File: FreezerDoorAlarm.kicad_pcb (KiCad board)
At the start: 2 copper layers, 64 x 35 mm, 36 parts, among them J1 Barrel_Jack, J2 Conn_01x02_Female, J3 Conn_01x01, J4 Conn_01x01, Q1 MMBT3906, Q2 MMBT3904, Q3 MMBT3906, Q4 MMBT3904, Q5 BSS138, Q6 MMBT3906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

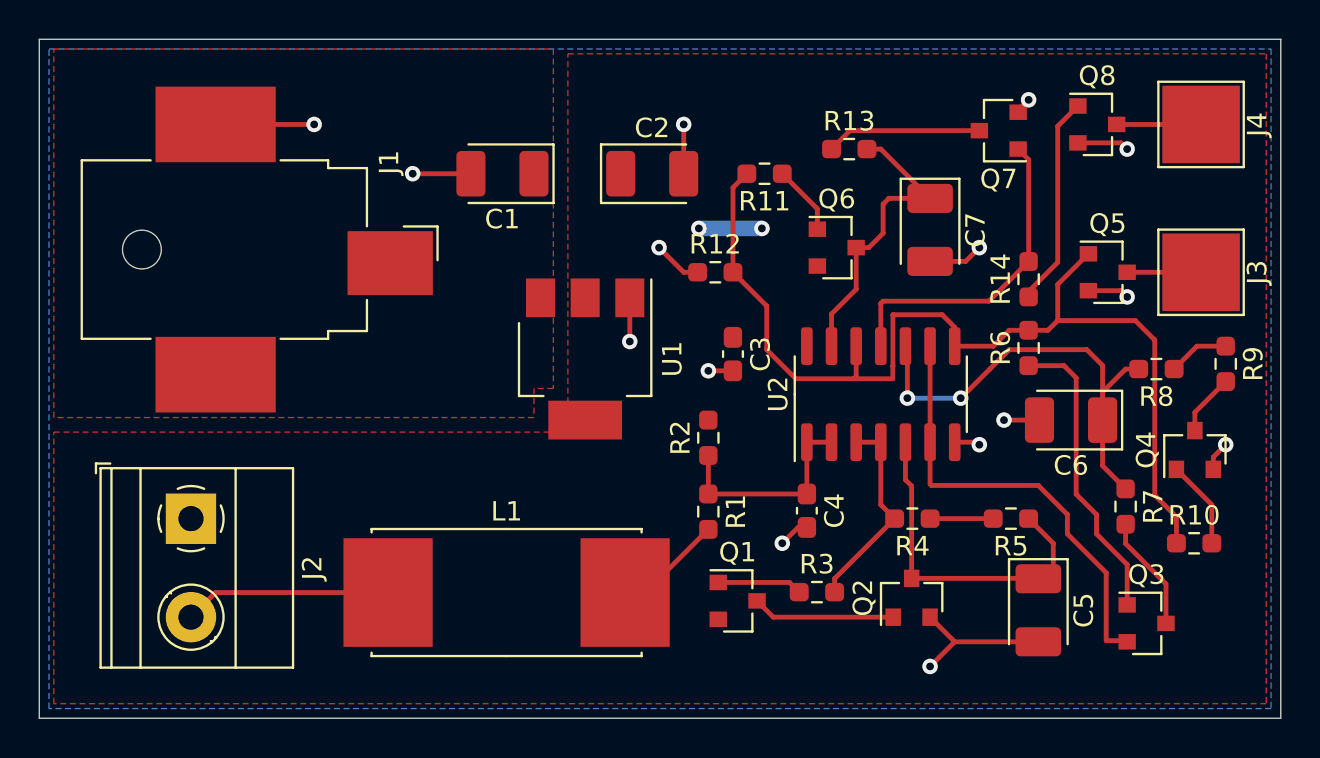
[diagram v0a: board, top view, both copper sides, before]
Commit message: Where large/fast currents are expected to flow (Q2/C5, U2 bypass) loop area has been reduced.
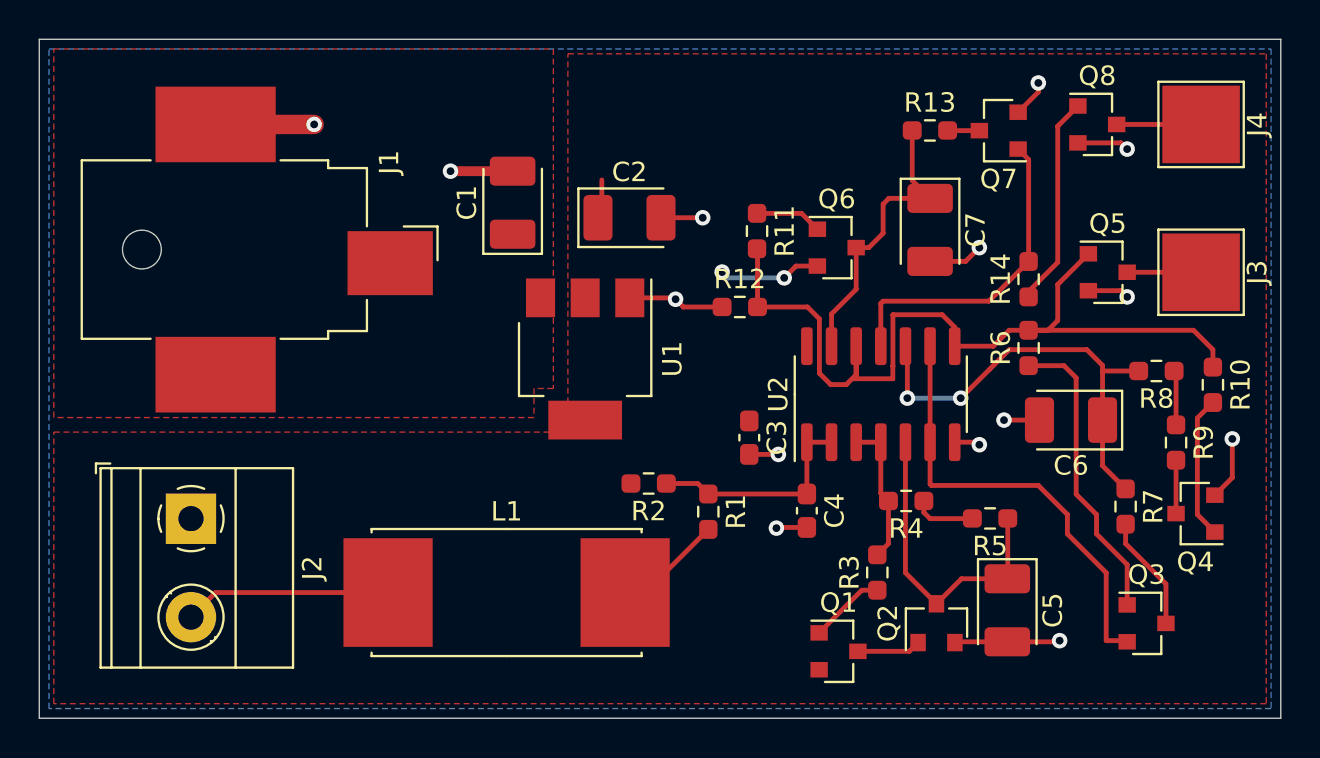
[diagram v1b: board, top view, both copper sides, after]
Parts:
- moved R10 8.22 mm to (136.5, 85.8), turned to 270 degrees
- moved Q1 5.81 mm to (117.2, 99.5)
- moved R9 4.80 mm to (134.6, 88.8)
- moved C3 4.39 mm to (112.6, 88.5)
- moved R13 4.27 mm to (121.9, 72.7)
- moved R2 3.88 mm to (107.4, 90.9), turned to 180 degrees
- moved Q4 3.28 mm to (135.6, 92.5), turned to 180 degrees
- moved R3 3.27 mm to (119.2, 95.5), turned to 90 degrees
- moved R11 2.98 mm to (113.0, 77.9), turned to 270 degrees
- moved C2 2.55 mm to (106.4, 77.2)
- moved R12 2.19 mm to (112.1, 81.8)
- moved Q2 1.83 mm to (122.2, 98.1)
- moved C5 1.60 mm to (125.9, 97.4)
- moved C1 1.58 mm to (100.4, 76.4), turned to 90 degrees
- moved R5 1.08 mm to (125.0, 92.7)
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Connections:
- R13 pad 1: Net-(Q7-Pad3) -> Net-(C7-Pad1)
- R13 pad 2: Net-(C7-Pad1) -> Net-(Q7-Pad3)
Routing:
- net Net-(Q5-Pad1): track 53.0 -> 45.3 mm
- net Net-(Q7-Pad3): track 8.01 -> 1.64 mm
- net +5V: track 3.25 -> 7.44 mm
- net Net-(Q1-Pad3): track 7.37 -> 3.29 mm
- net Net-(R3-Pad2): track 10.6 -> 7.48 mm
- net Net-(Q4-Pad1): track 4.57 -> 7.38 mm
- net Net-(C5-Pad1): track 17.3 -> 16.3 mm
- net GNDD: track 39.4 -> 39.9 mm, vias 15 -> 14
